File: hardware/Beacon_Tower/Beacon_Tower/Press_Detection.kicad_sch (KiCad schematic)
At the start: 9 parts, among them U201 PI4IOE5V6534Q

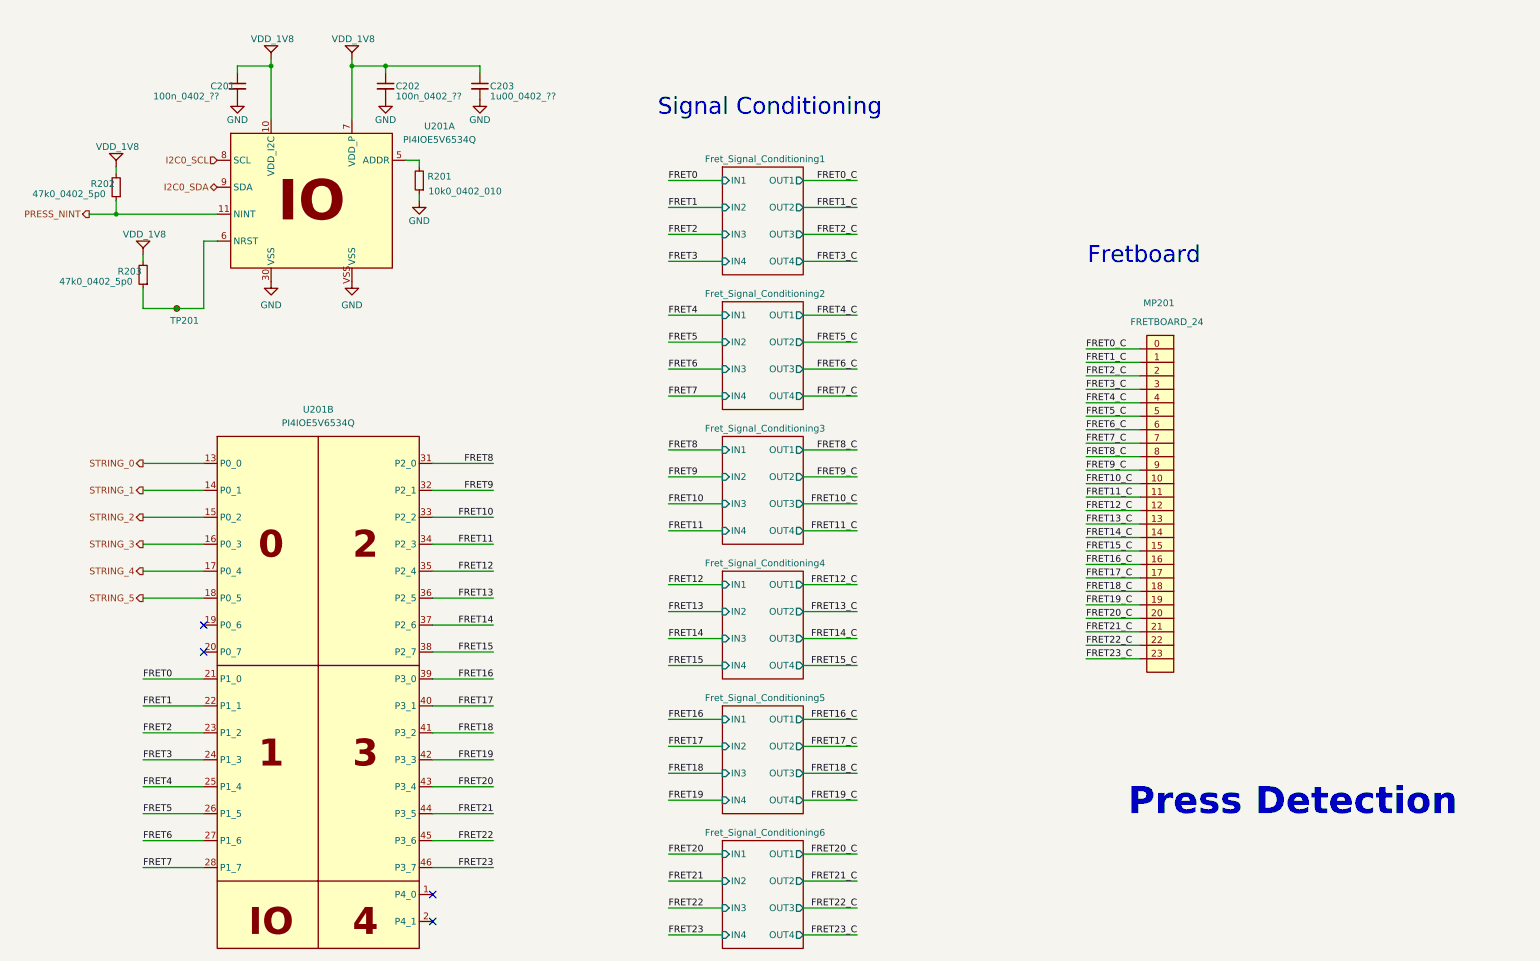
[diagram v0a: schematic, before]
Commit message: Started assigning footprints. Tweaking schematic.
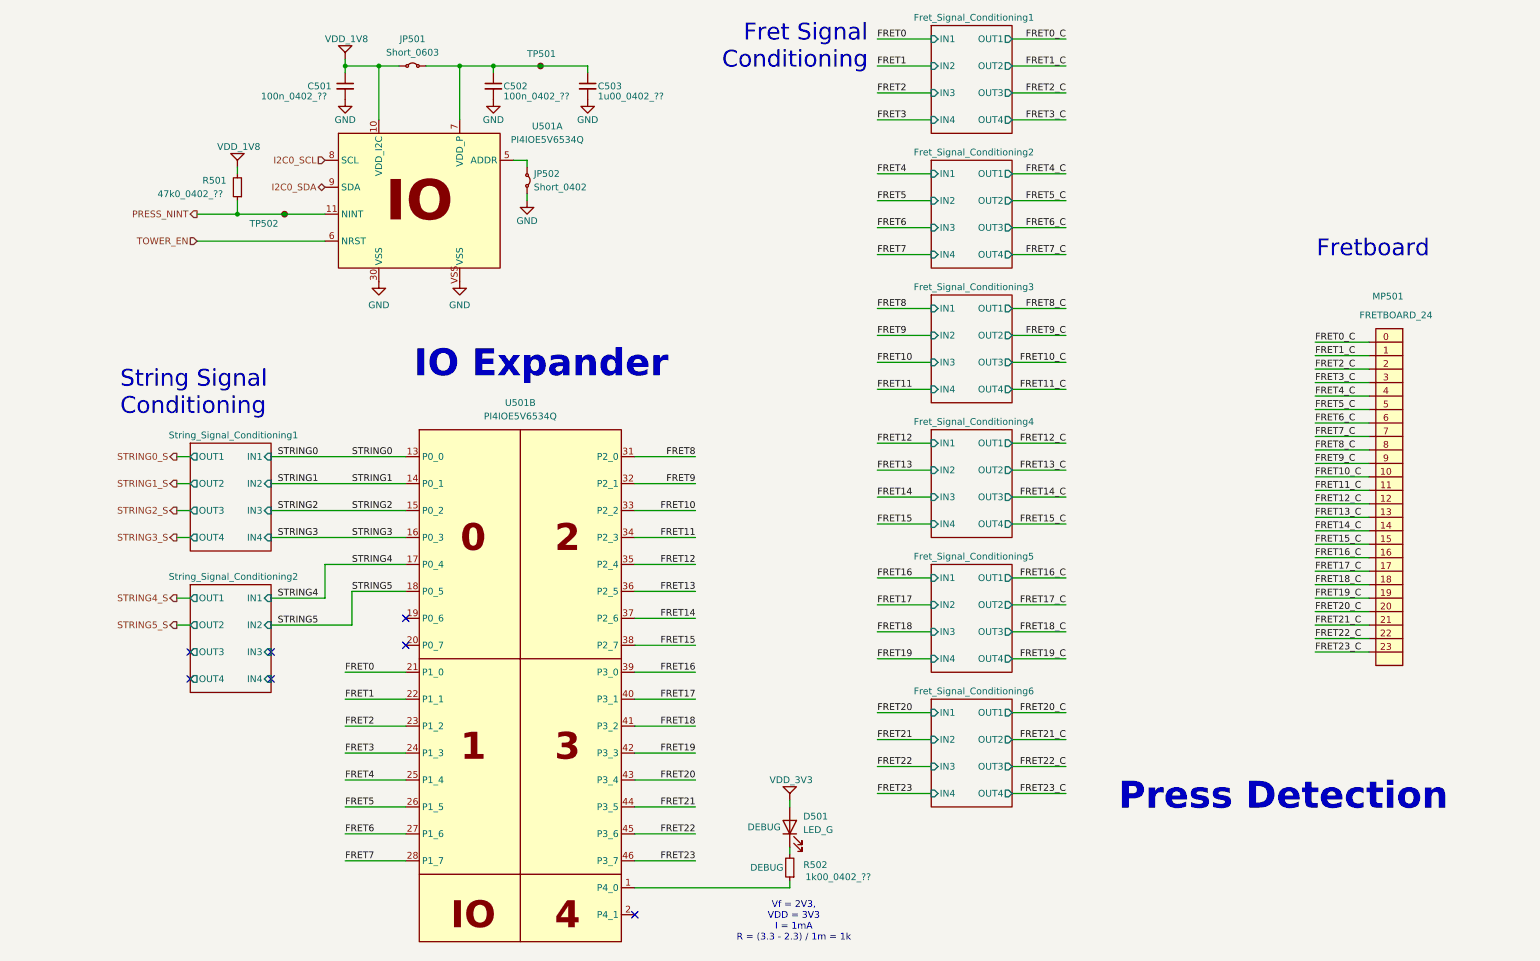
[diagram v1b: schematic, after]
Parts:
- removed R201: 10k0_0402_010, Footprint_Library:0402_1005Metric_Handsolder, symbol Device:R_Small
- removed R203: 47k0_0402_5p0, Footprint_Library:0603_1608Metric_Handsolder, symbol Device:R_Small
- removed TP201: TestPoint_Small, symbol Connector:TestPoint_Small
- removed U201: PI4IOE5V6534Q, symbol CUSTOM_LIBRARY:PI4IOE5V6534Q
- added D501: LED_G, symbol Device:LED
- added JP501: Short_0603, symbol Jumper:Jumper_2_Small_Bridged
- added JP502: Short_0402, CUSTOM_FOOTPRINTS:Jumper_0402, symbol Jumper:Jumper_2_Small_Bridged
- added R502: 1k00_0402_??, Resistor_SMD:R_0402_1005Metric, symbol Device:R_Small
- added TP501, TP502: TestPoint_Small, TestPoint:TestPoint_Pad_D2.0mm, symbol Connector:TestPoint_Small
- added U501: PI4IOE5V6534Q, CUSTOM_FOOTPRINTS:TQFN46_ZLW_DIO, symbol CUSTOM_LIBRARY:PI4IOE5V6534Q
- C501: renamed from C201; footprint (none) -> Capacitor_SMD:C_0402_1005Metric
- C502: renamed from C202; footprint (none) -> Capacitor_SMD:C_0402_1005Metric
- C503: renamed from C203; footprint (none) -> Capacitor_SMD:C_0402_1005Metric
- R501: renamed from R202; value 47k0_0402_5p0 -> 47k0_0402_??; footprint Footprint_Library:0603_1608Metric_Handsolder -> Resistor_SMD:R_0402_1005Metric
- renumbered MP201 to MP501
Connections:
- net FRET0: now also U501.21 (P1_0)
- net FRET1: now also U501.22 (P1_1)
- net FRET10: now also U501.33 (P2_2)
- net FRET11: now also U501.34 (P2_3)
- net FRET12: now also U501.35 (P2_4)
- net FRET13: now also U501.36 (P2_5)
- net FRET14: now also U501.37 (P2_6)
- net FRET15: now also U501.38 (P2_7)
- net FRET16: now also U501.39 (P3_0)
- net FRET17: now also U501.40 (P3_1)
- net FRET18: now also U501.41 (P3_2)
- net FRET19: now also U501.42 (P3_3)
- net FRET2: now also U501.23 (P1_2)
- net FRET20: now also U501.43 (P3_4)
- net FRET21: now also U501.44 (P3_5)
- net FRET22: now also U501.45 (P3_6)
- net FRET23: now also U501.46 (P3_7)
- net FRET3: now also U501.24 (P1_3)
- net FRET4: now also U501.25 (P1_4)
- net FRET5: now also U501.26 (P1_5)
- net FRET6: now also U501.27 (P1_6)
- net FRET7: now also U501.28 (P1_7)
- net FRET8: now also U501.31 (P2_0)
- net FRET9: now also U501.32 (P2_1)
- net GND: now also JP502.2 (B), U501.30 (VSS), U501.VSS
- net I2C0_SCL: now also U501.8 (SCL)
- net I2C0_SDA: now also U501.9 (SDA)
- net PRESS_NINT: now also TP502.1, U501.11 (NINT)
- net VDD_1V8: now also JP501.1 (A), U501.10 (VDD_I2C); no longer C502.1, C503.1
- new net: R502.1, U501.1 (P4_0)
- new net: D501.1 (K), R502.2
- new net: JP502.1 (A), U501.5 (ADDR)
- new net: C502.1, C503.1, JP501.2 (B), TP501.1, U501.7 (VDD_P)
- new net STRING0: U501.13 (P0_0)
- new net STRING1: U501.14 (P0_1)
- new net STRING2: U501.15 (P0_2)
- new net STRING3: U501.16 (P0_3)
- new net STRING4: U501.17 (P0_4)
- new net STRING5: U501.18 (P0_5)
- new net TOWER_EN: U501.6 (NRST)
- new net VDD_3V3: D501.2 (A)
- no-connect marks 4 -> 7
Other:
- added sheet String_Signal_Conditioning1 (String_Signal_Conditioning.kicad_sch)
- added sheet String_Signal_Conditioning2 (String_Signal_Conditioning.kicad_sch)
- note added: "Fret Signal Conditioning"
- note added: "IO Expander"
- note added: "String Signal Conditioning"
- note added: "Vf = 2V3, VDD = 3V3 I = 1mA R = (3.3 - 2.3) / 1m = 1k"
- note removed: "Signal Conditioning"
- moved on the sheet: C501, C502, C503, MP501, R501
